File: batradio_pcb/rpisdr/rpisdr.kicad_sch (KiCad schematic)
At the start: 18 parts, among them J1 RPI_header, J2 Conn_01x03, J3 Conn_01x03, U1 ldln025, U7 ldln025, U8 MCP4821

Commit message: Update rpi_adc_stream
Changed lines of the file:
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@@
     (effects (font (size 1.27 1.27)) (justify left bottom))
   )
-  (text "3 volt voor microfoon" (at 78.74 162.56 0)
+  (text "3 volt voor microfoon" (at 55.88 69.85 0)
     (effects (font (size 1.27 1.27)) (justify left bottom))
   )

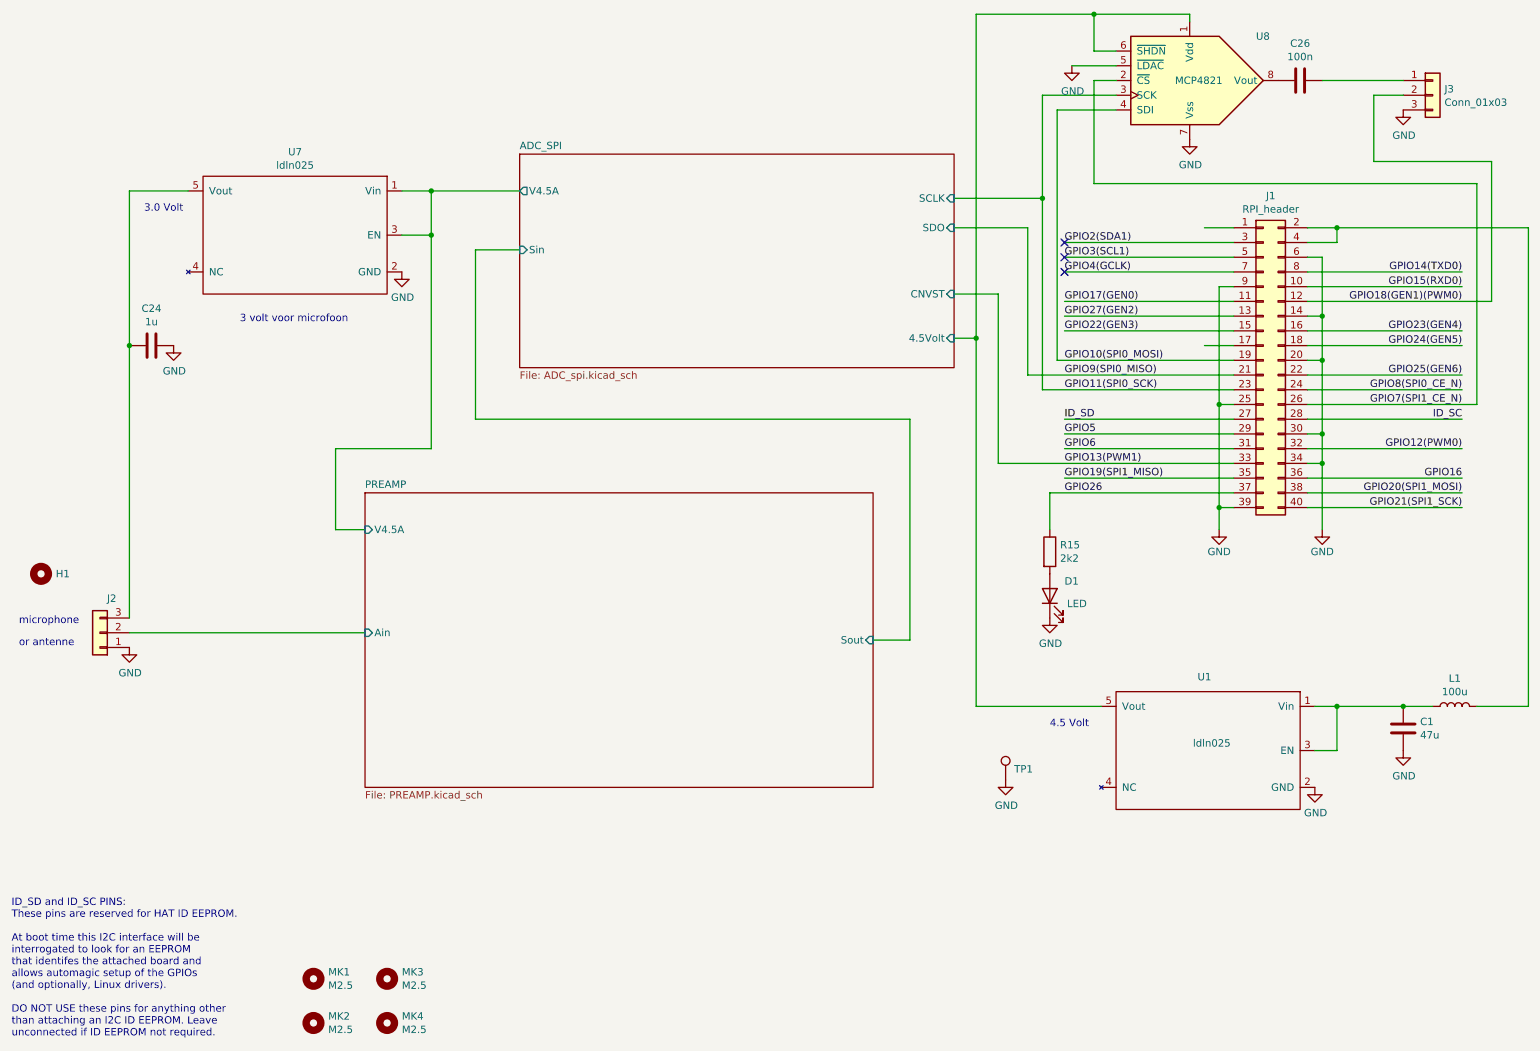
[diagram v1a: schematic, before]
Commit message: Corrected schematic and added mykicadlibs
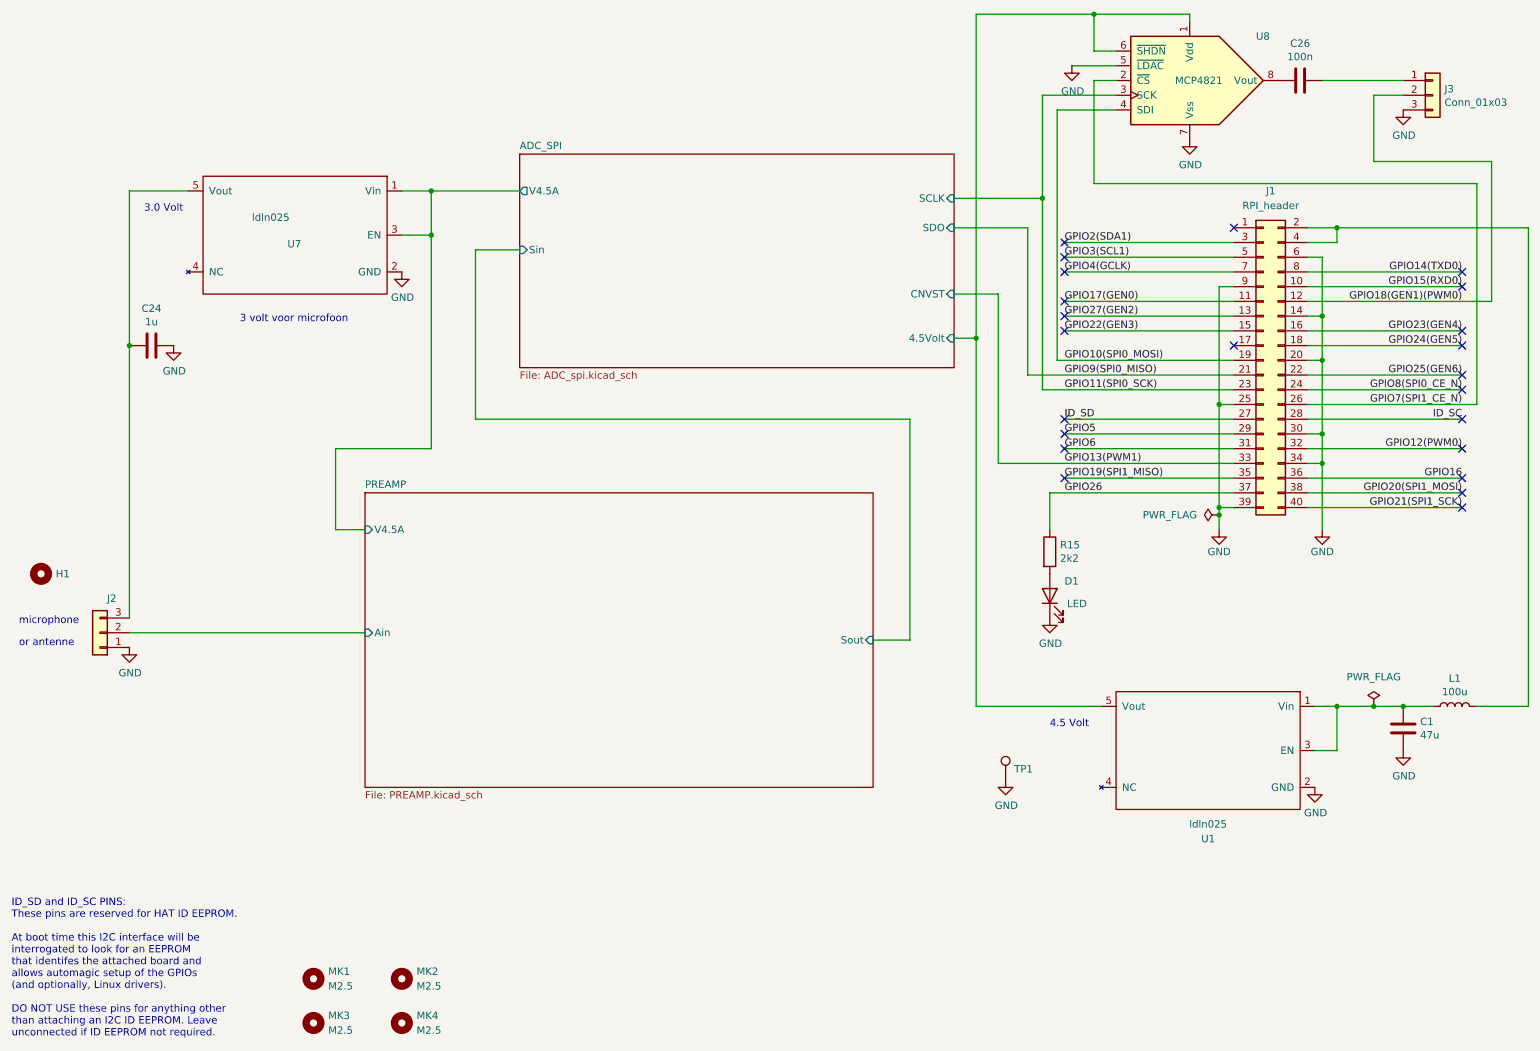
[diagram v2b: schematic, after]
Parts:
- removed J1: RPI_header, Connector_PinSocket_2.54mm:PinSocket_2x20_P2.54mm_Vertical, symbol rpisdr-rescue:RPI_header-mylib
- removed MK1, MK2, MK3, MK4: M2.5, MountingHole:MountingHole_2.7mm_M2.5, symbol rpisdr-rescue:Mounting_Hole-Mechanical-mylib
- removed U1, U7: ldln025, Package_TO_SOT_SMD:SOT-23-5, symbol rpisdr-rescue:ldln025-mylib
- added J1: RPI_header, Connector_PinHeader_2.54mm:PinHeader_2x20_P2.54mm_Vertical, symbol mylibxx:RPI_header
- added MK1, MK2, MK3, MK4: M2.5, MountingHole:MountingHole_2.7mm_M2.5, symbol mylibxx:Mounting_Hole-Mechanical
- added U1, U7: ldln025, Package_TO_SOT_SMD:SOT-23-5, symbol mylibxx:ldln025
- C24: footprint Capacitor_SMD:C_1206_3216Metric_Pad1.42x1.75mm_HandSolder -> Capacitor_SMD:C_1206_3216Metric_Pad1.33x1.80mm_HandSolder
- C26: footprint Capacitor_SMD:C_0805_2012Metric_Pad1.15x1.40mm_HandSolder -> Capacitor_SMD:C_0805_2012Metric_Pad1.18x1.45mm_HandSolder
- R15: footprint Resistor_SMD:R_0805_2012Metric_Pad1.15x1.40mm_HandSolder -> Resistor_SMD:R_0805_2012Metric_Pad1.20x1.40mm_HandSolder
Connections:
- net ADC_SPI/4.5Volt: now also U1.5 (Vout)
- net ADC_SPI/V4.5A: now also U7.1 (Vin), U7.3 (EN)
- net GND: now also J1.14 (Pin_14), J1.20 (Pin_20), J1.25 (Pin_25), J1.30 (Pin_30), J1.34 (Pin_34), J1.39 (Pin_39), J1.6 (Pin_6), J1.9 (Pin_9), U1.2 (GND), U7.2 (GND)
- net GPIO10(SPI0_MOSI): now also J1.19 (Pin_19)
- net GPIO11(SPI0_SCK): now also J1.23 (Pin_23)
- net GPIO12(PWM0): now also J1.32 (Pin_32)
- net GPIO13(PWM1): now also J1.33 (Pin_33)
- net GPIO14(TXD0): now also J1.8 (Pin_8)
- net GPIO15(RXD0): now also J1.10 (Pin_10)
- net GPIO16: now also J1.36 (Pin_36)
- net GPIO17(GEN0): now also J1.11 (Pin_11)
- net GPIO18(GEN1)(PWM0): now also J1.12 (Pin_12)
- net GPIO19(SPI1_MISO): now also J1.35 (Pin_35)
- net GPIO2(SDA1): now also J1.3 (Pin_3)
- net GPIO20(SPI1_MOSI): now also J1.38 (Pin_38)
- net GPIO21(SPI1_SCK): now also J1.40 (Pin_40)
- net GPIO22(GEN3): now also J1.15 (Pin_15)
- net GPIO23(GEN4): now also J1.16 (Pin_16)
- net GPIO24(GEN5): now also J1.18 (Pin_18)
- net GPIO25(GEN6): now also J1.22 (Pin_22)
- net GPIO26: now also J1.37 (Pin_37)
- net GPIO27(GEN2): now also J1.13 (Pin_13)
- net GPIO3(SCL1): now also J1.5 (Pin_5)
- net GPIO4(GCLK): now also J1.7 (Pin_7)
- net GPIO5: now also J1.29 (Pin_29)
- net GPIO6: now also J1.31 (Pin_31)
- net GPIO7(SPI1_CE_N): now also J1.26 (Pin_26)
- net GPIO8(SPI0_CE_N): now also J1.24 (Pin_24)
- net GPIO9(SPI0_MISO): now also J1.21 (Pin_21)
- net ID_SC: now also J1.28 (Pin_28)
- net ID_SD: now also J1.27 (Pin_27)
- net at C1.1, L1.1: now also U1.1 (Vin), U1.3 (EN)
- net at L1.2: now also J1.2 (Pin_2), J1.4 (Pin_4)
- net at C24.2, J2.3 (Pin_3): now also U7.5 (Vout)
- no-connect marks 3 -> 23

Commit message: Corrected mylib library settings
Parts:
- J1: symbol mylibxx:RPI_header -> mylib:RPI_header
- MK1, MK2, MK3, MK4: symbol mylibxx:Mounting_Hole-Mechanical -> mylib:Mounting_Hole-Mechanical
- U1, U7: symbol mylibxx:ldln025 -> mylib:ldln025
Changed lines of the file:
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@@
 	)
 	(symbol
-		(lib_id "mylibxx:ldln025")
+		(lib_id "mylib:ldln025")
 		(at 68.58 52.07 0)
 		(mirror y)
@@
 	)
 	(symbol
-		(lib_id "mylibxx:Mounting_Hole-Mechanical")
+		(lib_id "mylib:Mounting_Hole-Mechanical")
 		(at 68.58 182.88 0)
 		(unit 1)
@@
 	)
 	(symbol
-		(lib_id "mylibxx:ldln025")
+		(lib_id "mylib:ldln025")
 		(at 226.06 140.97 0)
 		(mirror y)
@@
 	)
 	(symbol
-		(lib_id "mylibxx:RPI_header")
+		(lib_id "mylib:RPI_header")
 		(at 232.41 76.2 0)
 		(unit 1)
@@
 	)
 	(symbol
-		(lib_id "mylibxx:Mounting_Hole-Mechanical")
+		(lib_id "mylib:Mounting_Hole-Mechanical")
 		(at 83.82 182.88 0)
 		(unit 1)
@@
 	)
 	(symbol
-		(lib_id "mylibxx:Mounting_Hole-Mechanical")
+		(lib_id "mylib:Mounting_Hole-Mechanical")
 		(at 68.58 190.5 0)
 		(unit 1)
@@
 	)
 	(symbol
-		(lib_id "mylibxx:Mounting_Hole-Mechanical")
+		(lib_id "mylib:Mounting_Hole-Mechanical")
 		(at 83.82 190.5 0)
 		(unit 1)
